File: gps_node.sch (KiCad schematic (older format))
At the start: 24 parts

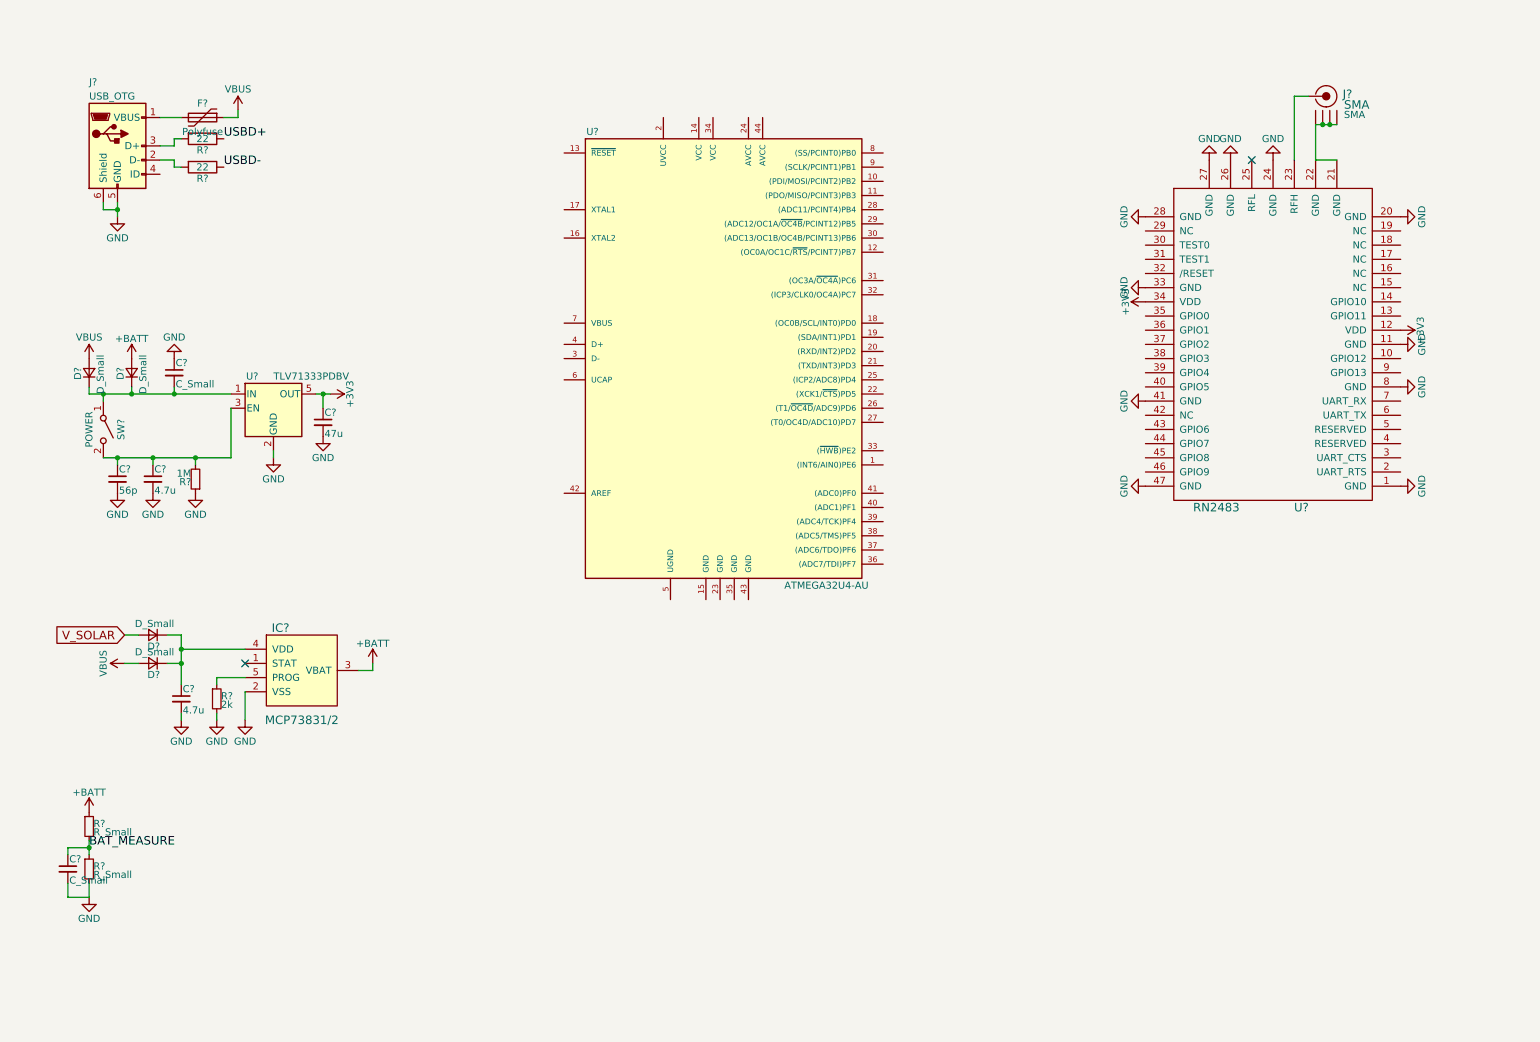
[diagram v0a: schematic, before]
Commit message: Add gps module
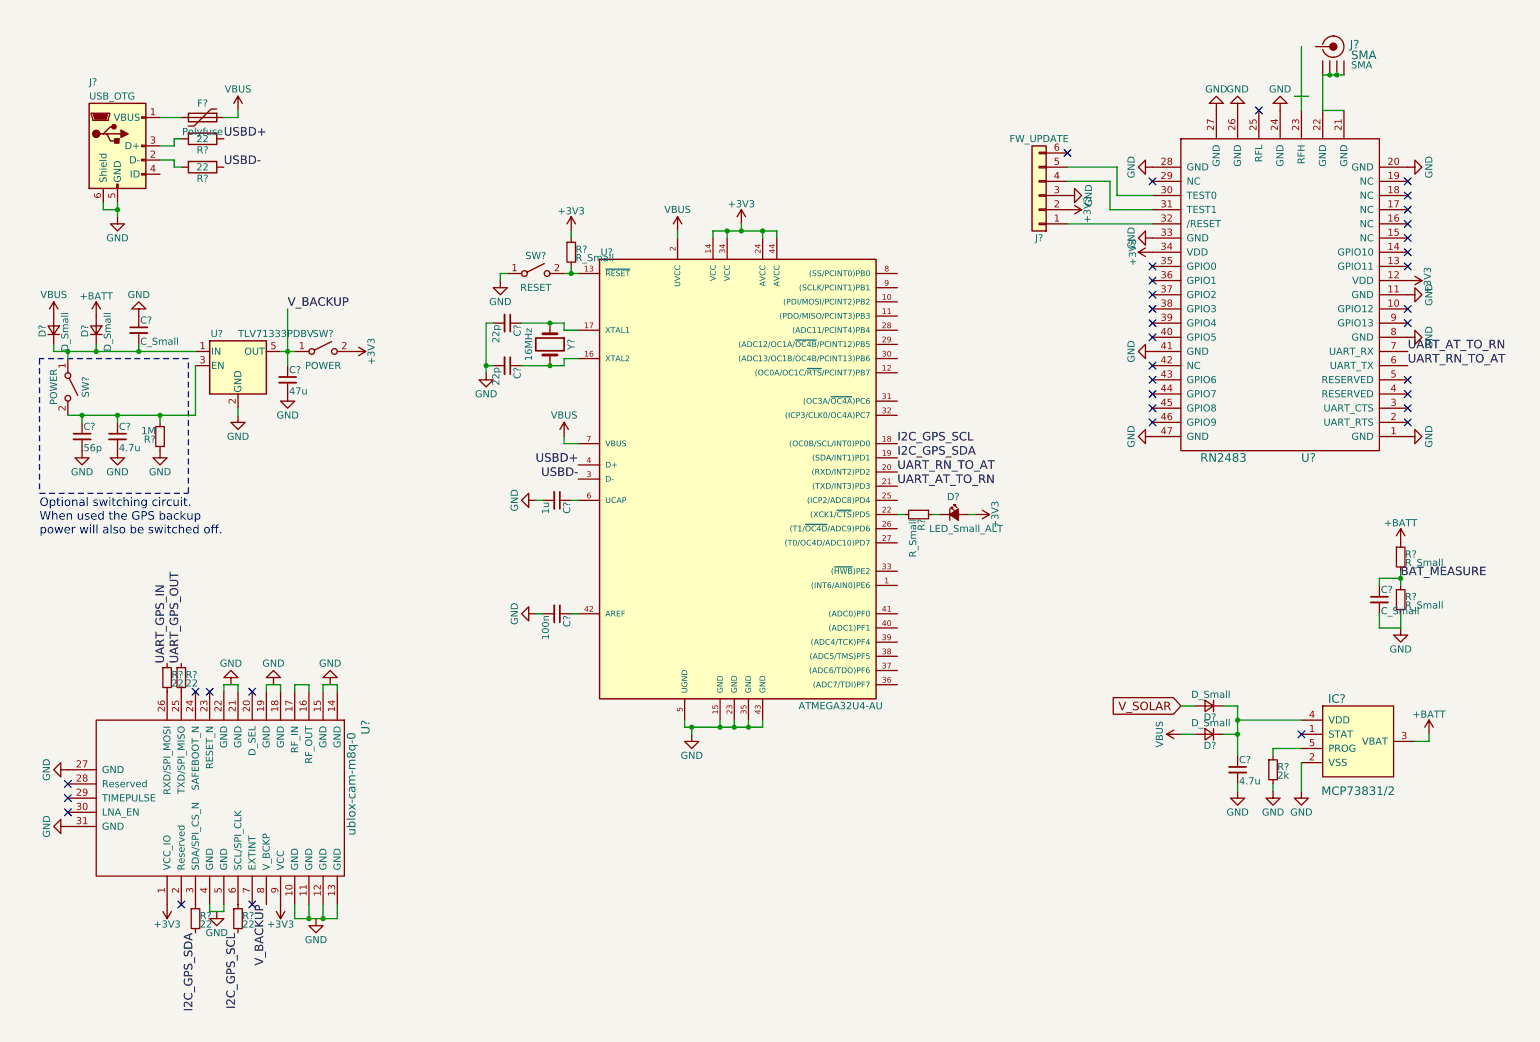
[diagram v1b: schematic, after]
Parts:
- added C? (x2): 22p, symbol C_Small
- added C?: 1u, symbol C_Small
- added C?: 100n, symbol C_Small
- added D?: LED_Small_ALT, symbol LED_Small_ALT
- added J?: FW_UPDATE, symbol Conn_01x06
- added R? (x2): R_Small, symbol R_Small
- added R? (x4): 22, symbol R_Small
- added SW?: RESET, symbol SW_SPST
- added SW?: POWER, symbol SW_SPST
- added U?: ublox-cam-m8q-0, symbol ublox-cam-m8q-0
- added Y?: 16MHz, symbol Crystal
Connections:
- net +3V3: now also U?.14 (VCC), U?.24 (AVCC), U?.34 (VCC), U?.44 (AVCC), D?.2 (A), J?.2 (Pin_2), R?.1, SW?.2 (B), U?.1 (VCC_IO), U?.9 (VCC); no longer C?.1, U?.5 (OUT)
- net GND: now also U?.15 (GND), U?.23 (GND), U?.35 (GND), U?.43 (GND), U?.5 (UGND), C?.2, C?.2, C?.2, C?.2, J?.3 (Pin_3), SW?.1 (A), U?.27 (GND), U?.31 (GND)
- net USBD+: now also U?.4 (D+)
- net USBD-: now also U?.3 (D-)
- net VBUS: now also U?.2 (UVCC), U?.7 (VBUS)
- net at U?.13 (~RESET~): now also R?.2, SW?.2 (B)
- net at U?.16 (XTAL2): now also C?.1, Y?.2
- net at U?.17 (XTAL1): now also C?.1, Y?.1
- net I2C_GPS_SCL: now reaches U?.18 ((OC0B/SCL/INT0)PD0)
- net I2C_GPS_SCL: now also R?.2
- net I2C_GPS_SDA: now reaches U?.19 ((SDA/INT1)PD1)
- net I2C_GPS_SDA: now also R?.2
- net UART_RN_TO_AT: now reaches U?.20 ((RXD/INT2)PD2)
- net UART_RN_TO_AT: now also U?.6 (UART_TX)
- net UART_AT_TO_RN: now reaches U?.21 ((TXD/INT3)PD3)
- net UART_AT_TO_RN: now also U?.7 (UART_RX)
- net at U?.22 ((XCK1/~CTS~)PD5): now also R?.2
- net at U?.42 (AREF): now also C?.1
- net at U?.6 (UCAP): now also C?.1
- net at U?.23 (RFH): no longer J?.1 (RF)
- net at U?.30 (TEST0): now also J?.5 (Pin_5)
- net at U?.31 (TEST1): now also J?.4 (Pin_4)
- net at U?.32 (/RESET): now also J?.1 (Pin_1)
- new net: D?.1 (K), R?.1
- new net: U?.10 (GND), U?.11 (GND), U?.12 (GND), U?.13 (GND)
- new net: U?.14 (GND), U?.15 (GND)
- new net: U?.16 (RF_OUT), U?.17 (RF_IN)
- new net: U?.18 (GND), U?.19 (GND)
- new net: U?.21 (GND), U?.22 (GND)
- new net: R?.2, U?.25 (TXD/SPI_MISO)
- new net: R?.2, U?.26 (RXD/SPI_MOSI)
- new net: R?.1, U?.3 (SDA/SPI_CS_N)
- new net: U?.4 (GND), U?.5 (GND)
- new net: R?.1, U?.6 (SCL/SPI_CLK)
- new net UART_GPS_IN: R?.1
- new net UART_GPS_OUT: R?.1
- new net V_BACKUP: C?.1, SW?.1 (A), U?.5 (OUT), U?.8 (V_BCKP)
- no-connect marks 2 -> 36
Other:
- note added: "Optional switching circuit.\nWhen used the GPS backup \npower will also be switched off."
- moved on the sheet: C?, D?, IC?, J?, R?, SW?, U?

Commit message: Add accelerometer
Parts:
- added C? (x2): 100n, symbol C_Small
- added IC?: MMA8452Q, symbol MMA8452Q
- added R? (x4): 22, symbol R_Small
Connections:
- net +3V3: now also C?.1, IC?.1 (VDDIO), IC?.14 (VDD)
- net BAT_MEASURE: now also U?.41 ((ADC0)PF0)
- net GND: now also C?.2, C?.2, IC?.10 (GND), IC?.12 (GND), IC?.5 (GND), IC?.7 (SA0)
- net I2C_GPS_SCL: now also R?.1
- net I2C_GPS_SDA: now also R?.1
- net UART_GPS_IN: now also U?.30 ((ADC13/OC1B/OC4B/PCINT13)PB6)
- net UART_GPS_OUT: now also U?.29 ((ADC12/OC1A/~OC4B~/PCINT12)PB5)
- new net: C?.1, IC?.2 (BYP)
- new net: IC?.4 (SCL), R?.2
- new net: IC?.6 (SDA), R?.2
- no-connect marks 36 -> 41
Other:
- note added: "Design based on:\nhttps://www.sparkfun.com/products/12587\nand the Sodaq One"

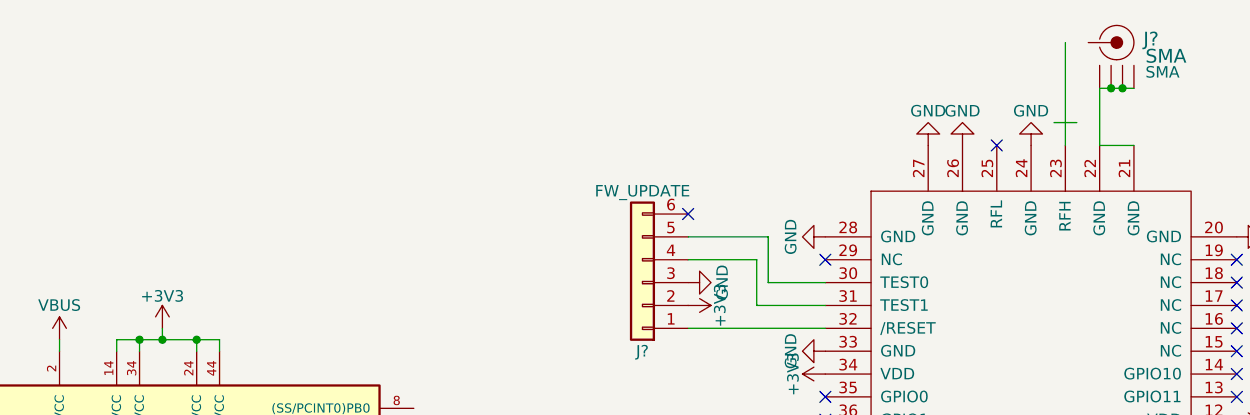
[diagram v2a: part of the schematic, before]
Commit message: Add connector for battery and solar panel
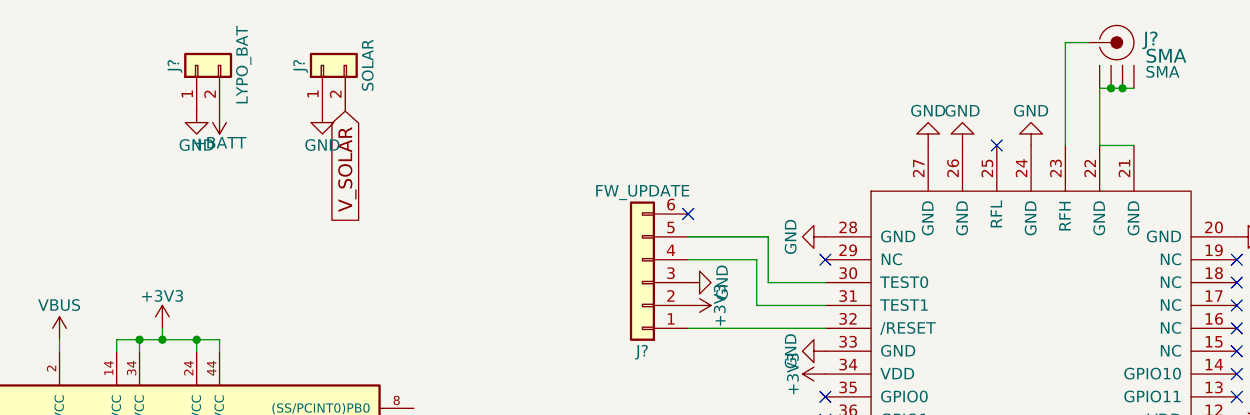
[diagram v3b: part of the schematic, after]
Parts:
- added J?: LYPO_BAT, symbol Conn_01x02
- added J?: SOLAR, symbol Conn_01x02
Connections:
- net +BATT: now also J?.2 (Pin_2)
- net GND: now also J?.1 (Pin_1), J?.1 (Pin_1)
- net V_SOLAR: now also J?.2 (Pin_2)
- net at U?.23 (RFH): now also J?.1 (RF)
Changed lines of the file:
@@
 	9650 1200 9650 750
-Wire Wire Line
-	9600 1100 9700 1100
 Wire Wire Line
 	10350 4450 10350 4550
@@
 Wire Wire Line
 	5700 6450 5750 6450
+$Comp
+L Conn_01x02 J?
+U 1 1 5A2DF363
+P 5850 850
+F 0 "J?" H 5850 950 50  0000 C CNN
+F 1 "LYPO_BAT" H 5850 650 50  0000 C CNN
+F 2 "" H 5850 850 50  0001 C CNN
+F 3 "" H 5850 850 50  0001 C CNN
+	1    5850 850
+	0    -1   -1   0
+$EndComp
+$Comp
+L Conn_01x02 J?
+U 1 1 5A2DF422
+P 6400 850
+F 0 "J?" H 6400 950 50  0000 C CNN
+F 1 "SOLAR" H 6400 650 50  0000 C CNN
+F 2 "" H 6400 850 50  0001 C CNN
+F 3 "" H 6400 850 50  0001 C CNN
+	1    6400 850
+	0    -1   -1   0
+$EndComp
+$Comp
+L GND #PWR?
+U 1 1 5A2DF88F
+P 5850 1050
+F 0 "#PWR?" H 5850 800 50  0001 C CNN
+F 1 "GND" H 5850 900 50  0000 C CNN
+F 2 "" H 5850 1050 50  0001 C CNN
+F 3 "" H 5850 1050 50  0001 C CNN
+	1    5850 1050
+	1    0    0    -1
+$EndComp
+$Comp
+L GND #PWR?
+U 1 1 5A2DF905
+P 6400 1050
+F 0 "#PWR?" H 6400 800 50  0001 C CNN
+F 1 "GND" H 6400 900 50  0000 C CNN
+F 2 "" H 6400 1050 50  0001 C CNN
+F 3 "" H 6400 1050 50  0001 C CNN
+	1    6400 1050
+	1    0    0    -1
+$EndComp
+Text GLabel 6500 1050 3    60   Input ~ 0
+V_SOLAR
+$Comp
+L +BATT #PWR?
+U 1 1 5A2DFDB1
+P 5950 1050
+F 0 "#PWR?" H 5950 900 50  0001 C CNN
+F 1 "+BATT" H 5950 1190 50  0000 C CNN
+F 2 "" H 5950 1050 50  0001 C CNN
+F 3 "" H 5950 1050 50  0001 C CNN
+	1    5950 1050
+	-1   0    0    1
+$EndComp
+Wire Wire Line
+	9650 750  9750 750
 $EndSCHEMATC

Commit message: Connect accelerometer interrupts
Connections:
- net ACC_INT1: now reaches U?.8 ((SS/PCINT0)PB0)
- net ACC_INT1: now also R?.1
- net ACC_INT2: now reaches U?.9 ((SCLK/PCINT1)PB1)
- net ACC_INT2: now also R?.1
- net at IC?.11 (INT1): now also R?.2
- net at IC?.9 (INT2): now also R?.2
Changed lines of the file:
@@
 Wire Wire Line
 	9650 750  9750 750
+Wire Wire Line
+	5700 6700 5750 6700
+Wire Wire Line
+	5700 6800 5750 6800
+Text Label 5950 6800 0    60   ~ 0
+ACC_INT1
+Text Label 5950 6700 0    60   ~ 0
+ACC_INT2
+Text Label 6800 2350 0    60   ~ 0
+ACC_INT1
+Text Label 6800 2450 0    60   ~ 0
+ACC_INT2
 $EndSCHEMATC

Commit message: Add ICSP header
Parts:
- added J?: ICSP, symbol Conn_01x06
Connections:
- net +3V3: now also J?.2 (Pin_2)
- net ACC_INT1: now also U?.28 ((ADC11/PCINT4)PB4); no longer U?.8 ((SS/PCINT0)PB0)
- net ACC_INT2: now also U?.12 ((OC0A/OC1C/~RTS~/PCINT7)PB7); no longer U?.9 ((SCLK/PCINT1)PB1)
- net GND: now also J?.6 (Pin_6)
- net MISO: now reaches U?.10 ((PDI/MOSI/PCINT2)PB2)
- net MISO: now also J?.1 (Pin_1)
- net MOSI: now reaches U?.11 ((PDO/MISO/PCINT3)PB3)
- net MOSI: now also J?.4 (Pin_4)
- net RESET: now reaches R?.2, SW?.2 (B), U?.13 (~RESET~)
- net RESET: now also J?.5 (Pin_5)
- new net SCK: J?.3 (Pin_3), U?.9 ((SCLK/PCINT1)PB1)
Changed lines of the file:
@@
 Text Label 6800 3550 0    60   ~ 0
 I2C_GPS_SCL
-Text Notes 3200 1100 0    60   ~ 0
+Text Notes 550  800  0    60   ~ 0
 Design based on:\nhttps://www.sparkfun.com/products/12587\nand the Sodaq One
 Text Label 6800 2850 0    60   ~ 0
@@
 Text Label 5950 6700 0    60   ~ 0
 ACC_INT2
-Text Label 6800 2350 0    60   ~ 0
+Text Label 6800 2750 0    60   ~ 0
 ACC_INT1
+Text Label 6800 3050 0    60   ~ 0
+ACC_INT2
+$Comp
+L Conn_01x06 J?
+U 1 1 5A2E73E8
+P 4750 850
+F 0 "J?" H 4750 1150 50  0000 C CNN
+F 1 "ICSP" H 4750 450 50  0000 C CNN
+F 2 "" H 4750 850 50  0001 C CNN
+F 3 "" H 4750 850 50  0001 C CNN
+	1    4750 850
+	0    -1   -1   0
+$EndComp
+Text Label 4550 1050 3    60   ~ 0
+MISO
+$Comp
+L +3V3 #PWR?
+U 1 1 5A2E7677
+P 4650 1050
+F 0 "#PWR?" H 4650 900 50  0001 C CNN
+F 1 "+3V3" H 4650 1190 50  0000 C CNN
+F 2 "" H 4650 1050 50  0001 C CNN
+F 3 "" H 4650 1050 50  0001 C CNN
+	1    4650 1050
+	-1   0    0    1
+$EndComp
+Text Label 4750 1050 3    60   ~ 0
+SCK
+Text Label 4850 1050 3    60   ~ 0
+MOSI
+Text Label 4950 1050 3    60   ~ 0
+RESET
+$Comp
+L GND #PWR?
+U 1 1 5A2E7847
+P 5050 1050
+F 0 "#PWR?" H 5050 800 50  0001 C CNN
+F 1 "GND" H 5050 900 50  0000 C CNN
+F 2 "" H 5050 1050 50  0001 C CNN
+F 3 "" H 5050 1050 50  0001 C CNN
+	1    5050 1050
+	1    0    0    -1
+$EndComp
+Text Label 4550 2350 3    60   ~ 0
+RESET
+Text Label 6800 2650 0    60   ~ 0
+MOSI
 Text Label 6800 2450 0    60   ~ 0
-ACC_INT2
+SCK
+Text Label 6800 2550 0    60   ~ 0
+MISO
 $EndSCHEMATC
